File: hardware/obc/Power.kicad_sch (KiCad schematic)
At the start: 41 parts, among them Q403 IRLML2803, Q404 IRF7406PbF, U401 TPS7A4501DCQT, U403 TPS54226PWPRPWP14_2P31X2P46-L, U404 ADM1176-1ARMZ-R7, U405 BQ25886RGER

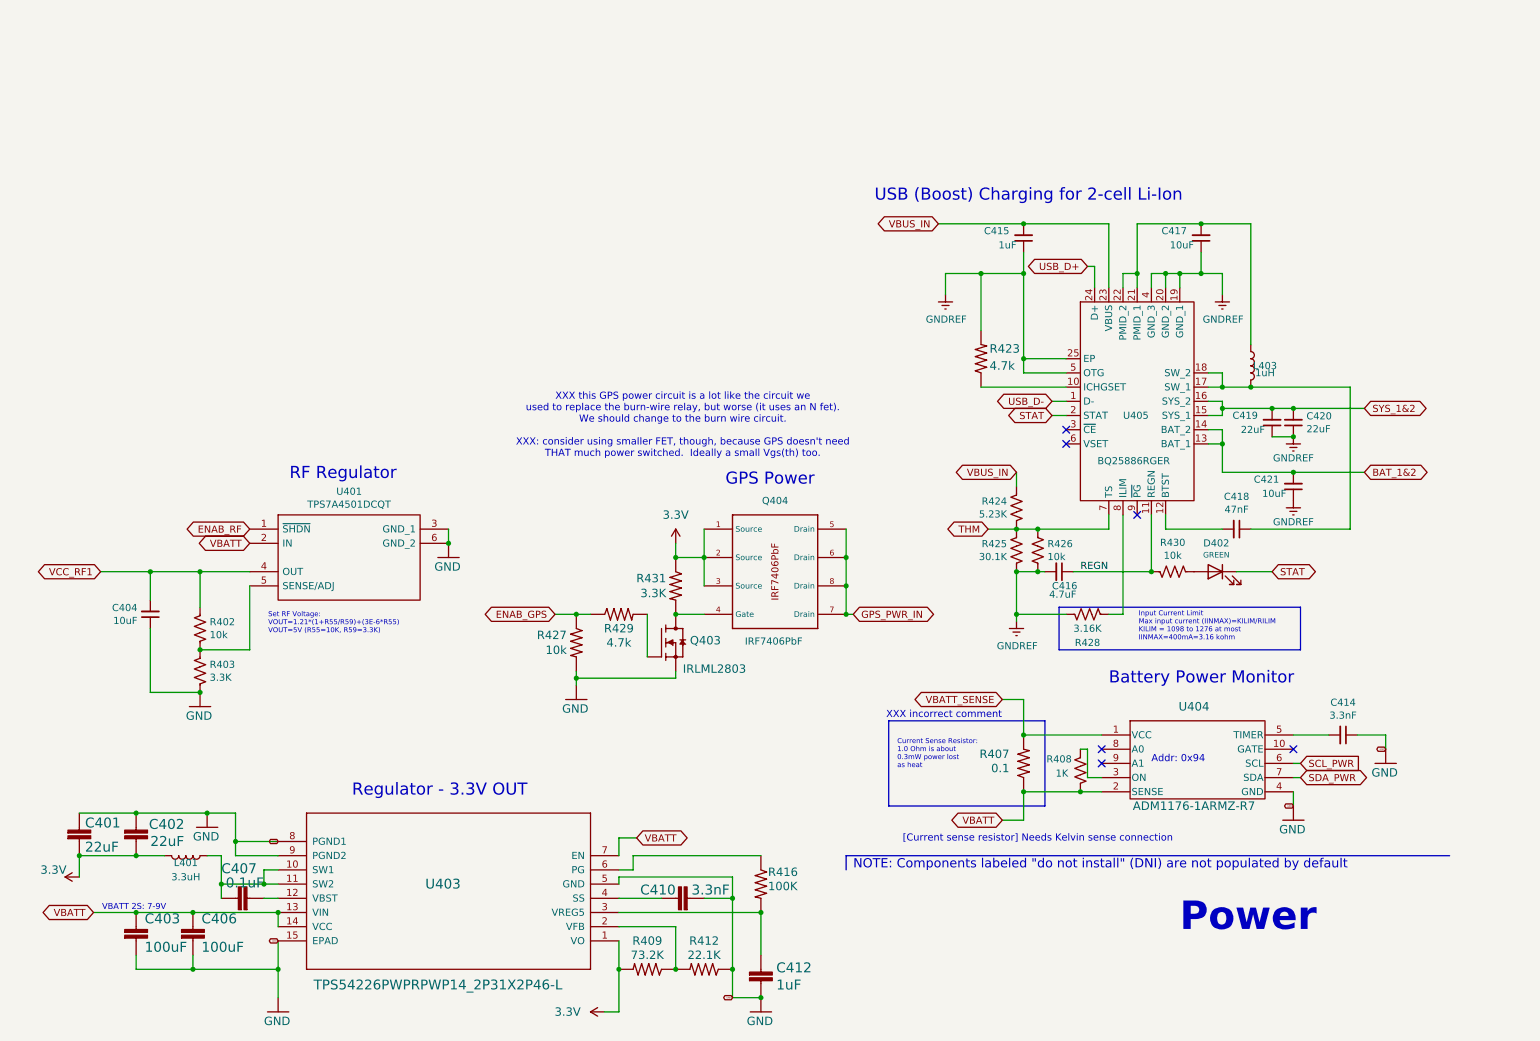
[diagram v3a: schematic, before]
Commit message: obc: Changed RF and 3.3V regulators from VBATT to VWATCHEDRAIL
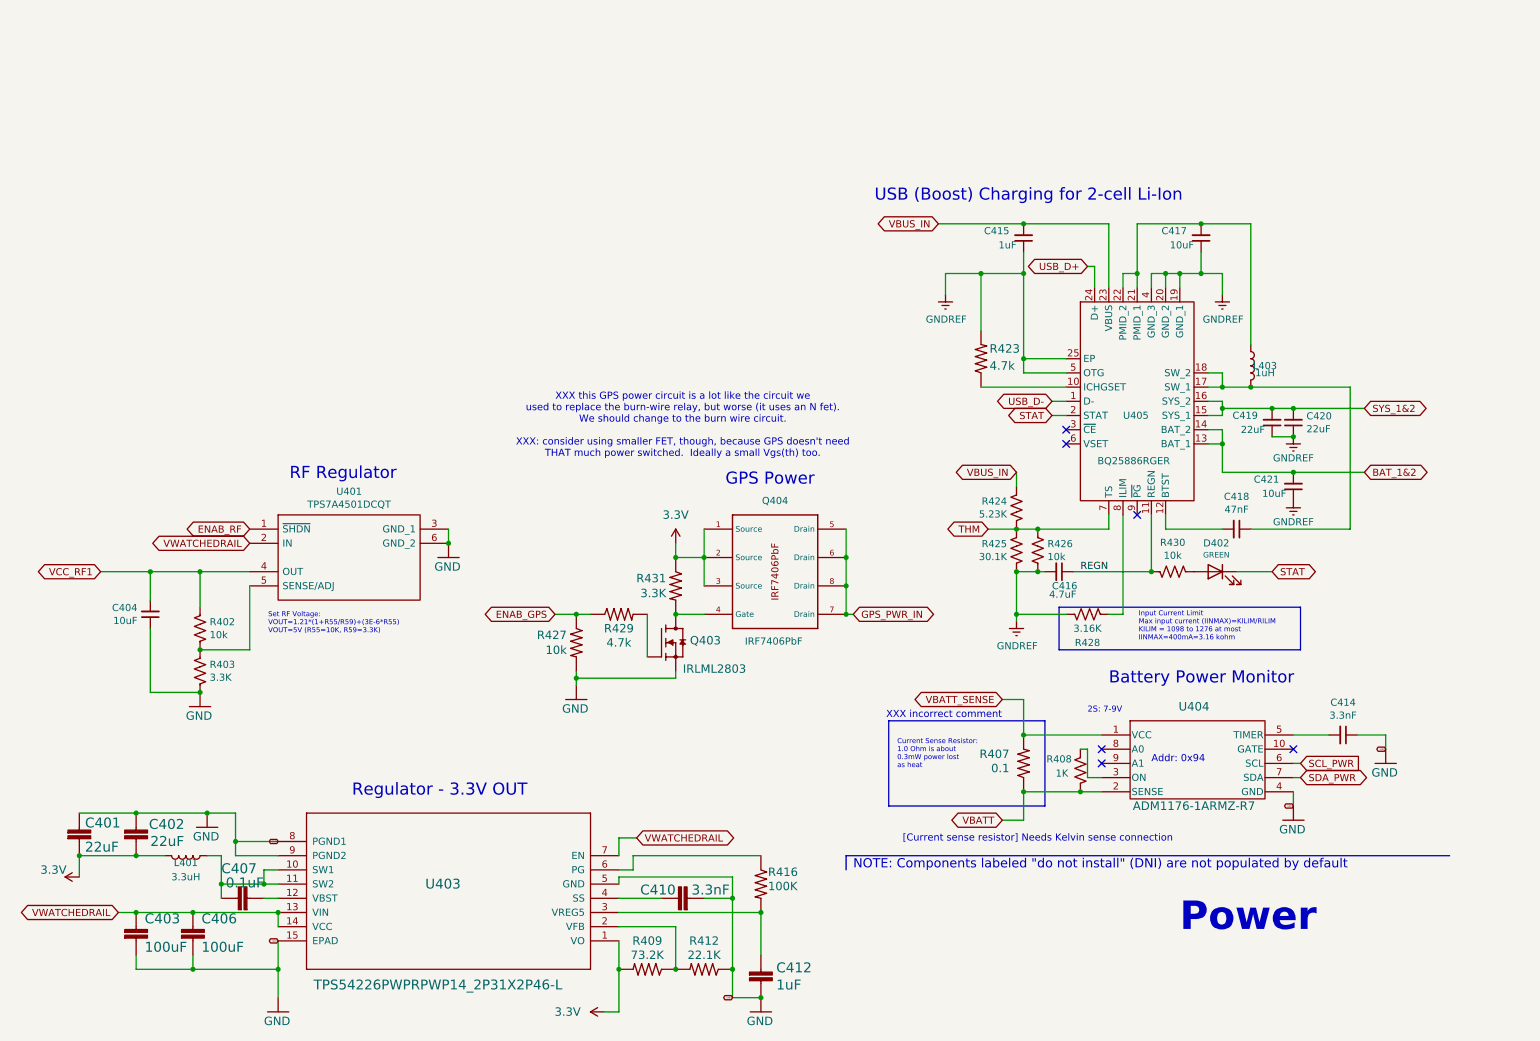
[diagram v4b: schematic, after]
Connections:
- net VBATT: no longer C403.1, C406.1, U401.2 (IN), U403.13 (VIN), U403.14 (VCC), U403.7 (EN)
- new net VWATCHEDRAIL: C403.1, C406.1, U401.2 (IN), U403.13 (VIN), U403.14 (VCC), U403.7 (EN)
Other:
- note added: "2S: 7-9V"
- note removed: "VBATT 2S: 7-9V"
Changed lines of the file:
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@@
 	(wire
 		(pts
-			(xy 33.02 179.07) (xy 25.4 179.07)
+			(xy 33.02 179.07) (xy 29.845 179.07)
 		)
 		(stroke
@@
 				(size 1.27 1.27)
 			)
-		)
-	)
-	(text "VBATT 2S: 7-9V"
-		(exclude_from_sim no)
-		(at 26.924 178.816 0)
-		(effects
-			(font
-				(size 1.0668 1.0668)
-			)
-			(justify left bottom)
 		)
 	)
@@
 		)
 	)
+	(text "2S: 7-9V"
+		(exclude_from_sim no)
+		(at 203.2 143.51 0)
+		(effects
+			(font
+				(size 1.0668 1.0668)
+			)
+			(justify left bottom)
+		)
+	)
 	(text "[Current sense resistor] Needs Kelvin sense connection"
 		(exclude_from_sim no)
@@
 		)
 	)
-	(global_label "VBATT"
+	(global_label "VWATCHEDRAIL"
 		(shape bidirectional)
 		(at 53.34 113.03 180)
@@
 		)
 	)
-	(global_label "VBATT"
-		(shape bidirectional)
-		(at 25.4 179.07 180)
-		(effects
-			(font
-				(size 1.27 1.27)
-			)
-			(justify right)
-		)
-		(property "Intersheetrefs" "${INTERSHEET_REFS}"
-			(at 25.4 179.07 0)
+	(global_label "VWATCHEDRAIL"
+		(shape bidirectional)
+		(at 29.845 179.07 180)
+		(effects
+			(font
+				(size 1.27 1.27)
+			)
+			(justify right)
+		)
+		(property "Intersheetrefs" "${INTERSHEET_REFS}"
+			(at 29.845 179.07 0)
 			(effects
 				(font
@@
 		)
 	)
-	(global_label "VBATT"
+	(global_label "VWATCHEDRAIL"
 		(shape bidirectional)
 		(at 122.555 165.735 0)

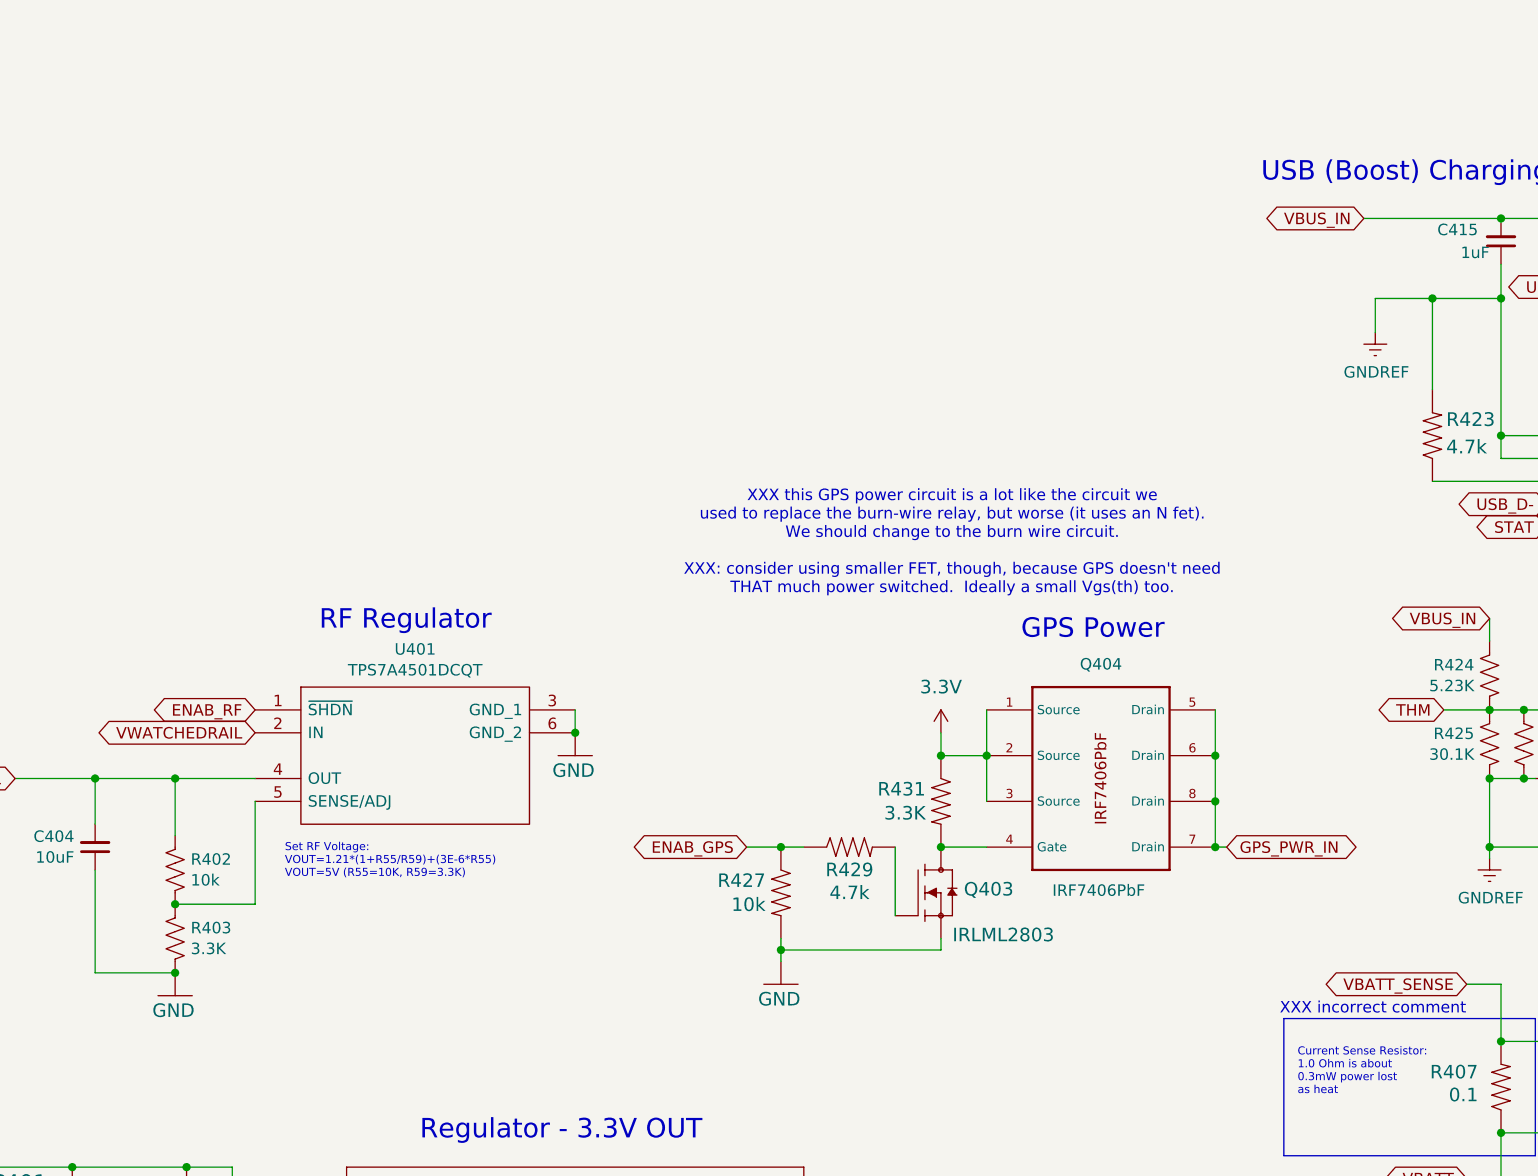
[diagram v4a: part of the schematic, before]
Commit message: obc: Fixed errors from design review
- Gave proper attribution on all pages
- Spread out components on Avionics page
- Changed GPS power circuit
- Added a DNP resistor in between VBATT and VWATCHEDRAIL
- Added various other part numbers on Power Supervisor and Watch Dog Page
- Changed Power Supervisor and Watch Dog Page to page 3
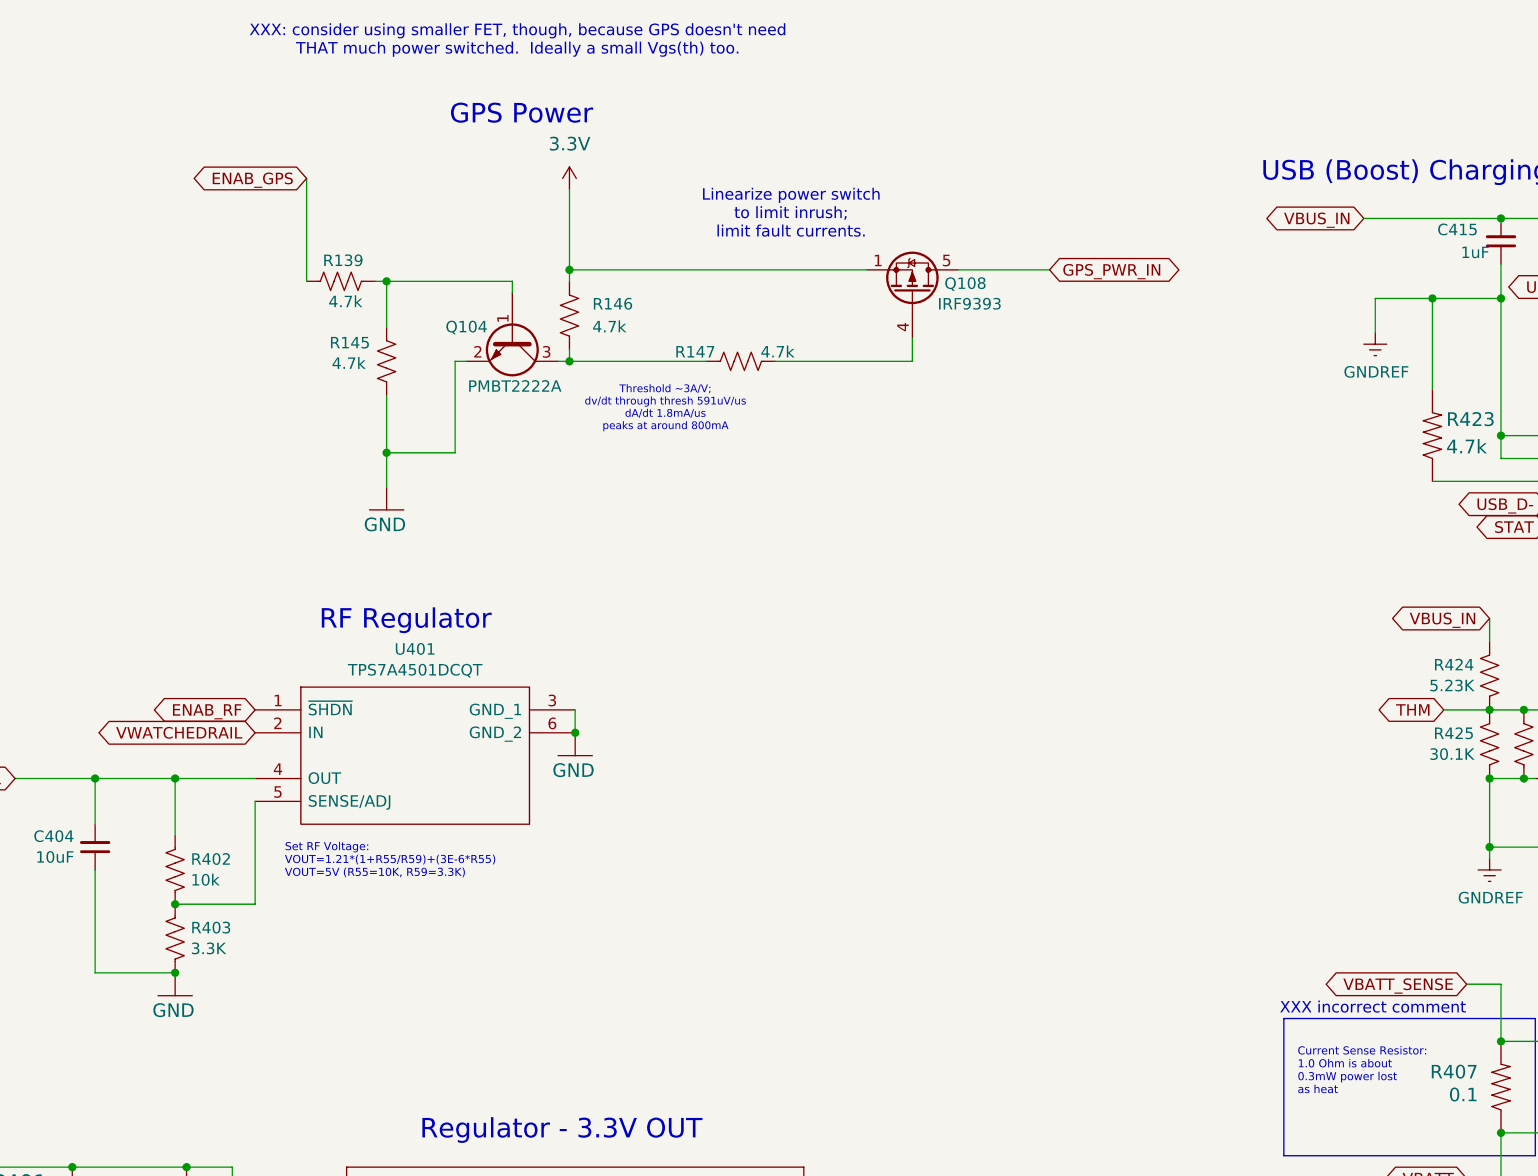
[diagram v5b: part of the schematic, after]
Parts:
- removed Q403: IRLML2803, Package_TO_SOT_SMD:SOT-23, symbol mainboard:IRLML2803TRPBF
- removed Q404: IRF7406PbF, Package_SO:SO-8_3.9x4.9mm_P1.27mm, symbol SSE_Symbols:MOSFET_IRF7406PbF
- removed R427: 10k, Resistor_SMD:R_0603_1608Metric, symbol mainboard:R-US_R0603
- removed R429: 4.7k, Resistor_SMD:R_0603_1608Metric, symbol mainboard:R-US_R0603
- removed R431: 3.3K, Resistor_SMD:R_0603_1608Metric, symbol mainboard:R-US_R0603
- added Q104: PMBT2222A, Package_TO_SOT_SMD:SOT-23, symbol Transistor_BJT:PMBT2222A
- added Q108: IRF9393, Package_SO:SOIC-8_3.9x4.9mm_P1.27mm, symbol Transistor_FET:IRF7404
- added R139, R145, R146, R147: 4.7k, Resistor_SMD:R_0603_1608Metric, symbol Device:R_US
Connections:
- net 3.3V: now also Q108.1 (S), Q108.2 (S), Q108.3 (S), R146.2
- net ENAB_GPS: now also R139.2
- net GND: now also Q104.2 (E), R145.1
- net GPS_PWR_IN: now also Q108.5 (D), Q108.6 (D), Q108.7 (D), Q108.8 (D)
- new net: Q104.1 (B), R139.1, R145.2
- new net: Q104.3 (C), R146.1, R147.1
- new net: Q108.4 (G), R147.2
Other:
- note added: "Linearize power switch to limit inrush; limit fault currents."
- note added: "Threshold ~3A/V; dv/dt through thresh 591uV/us dA/dt 1.8mA/us peaks at around 800mA"
- note added: "XXX: consider using smaller FET, though, because GPS doesn't need THAT much power switched. Ideally a small Vgs(th) too."
- note removed: "XXX this GPS power circuit is a lot like the circuit we used to replace the burn-wire relay, but worse (it uses an N fet). We should change to the burn wire circuit. XXX: consider using smaller FET, though, because GPS doesn't need THAT much power switched. Ideally a small Vgs(th) too."
- company: Ruchir Kavulli, Michael Lyle -> Ruchir Kavulli, Luke Titi, Michael Lyle
